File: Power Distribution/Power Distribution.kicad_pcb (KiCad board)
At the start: 4 copper layers, 60 x 82 mm, 81 parts, among them J1 Batt_Connector, J2 Motor Connector 1, J3 Motor Connector 2, J4 Motor Connector 3, J5 Motor Connector 3, U1 TPS552892RYQR, U2 TPS552892RYQR, U3 TPS552892RYQR, U4 TPS552892RYQR

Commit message: fixed via's
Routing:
- added copper zone on F.Cu, net Net-(U1-EXTVCC)
- added copper zone on F.Cu, net Net-(U3-EXTVCC)
- added copper zone on F.Cu, net Net-(U4-EXTVCC)

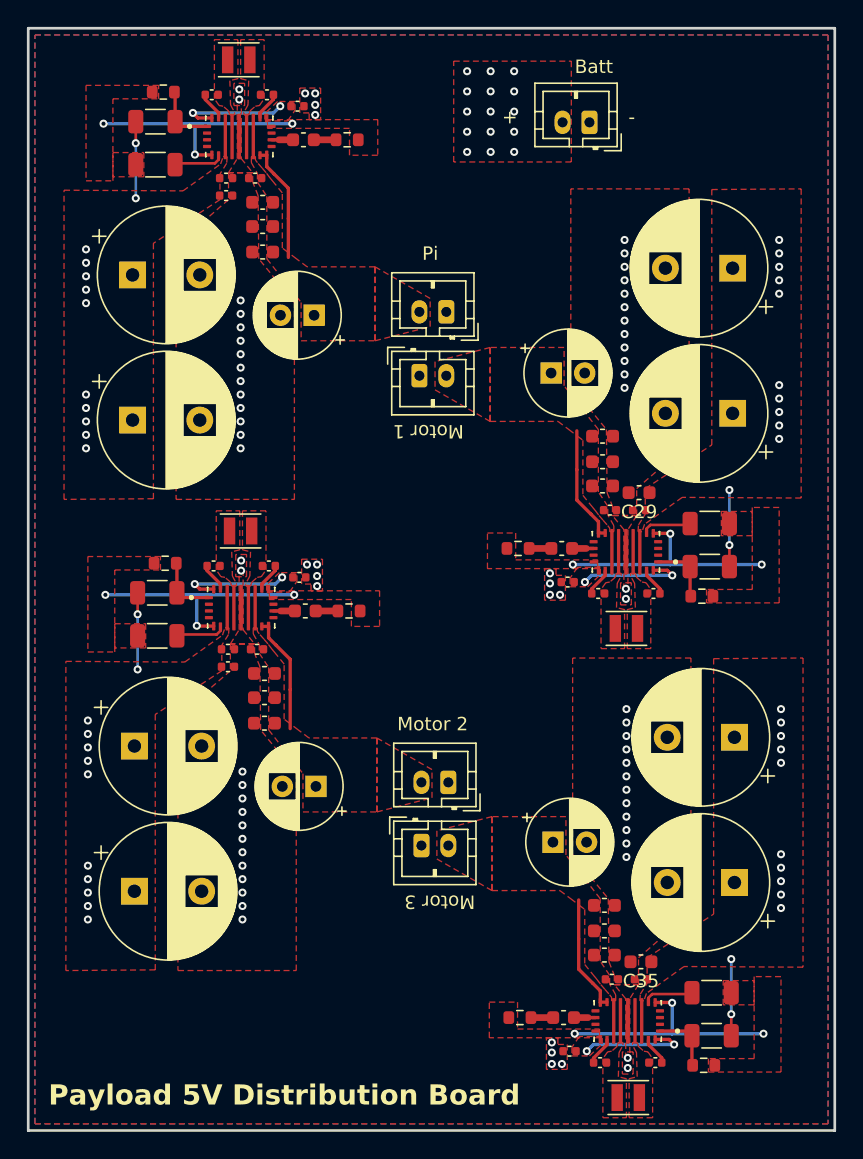
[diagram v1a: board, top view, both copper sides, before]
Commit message: added fabs and fixed i2c loop
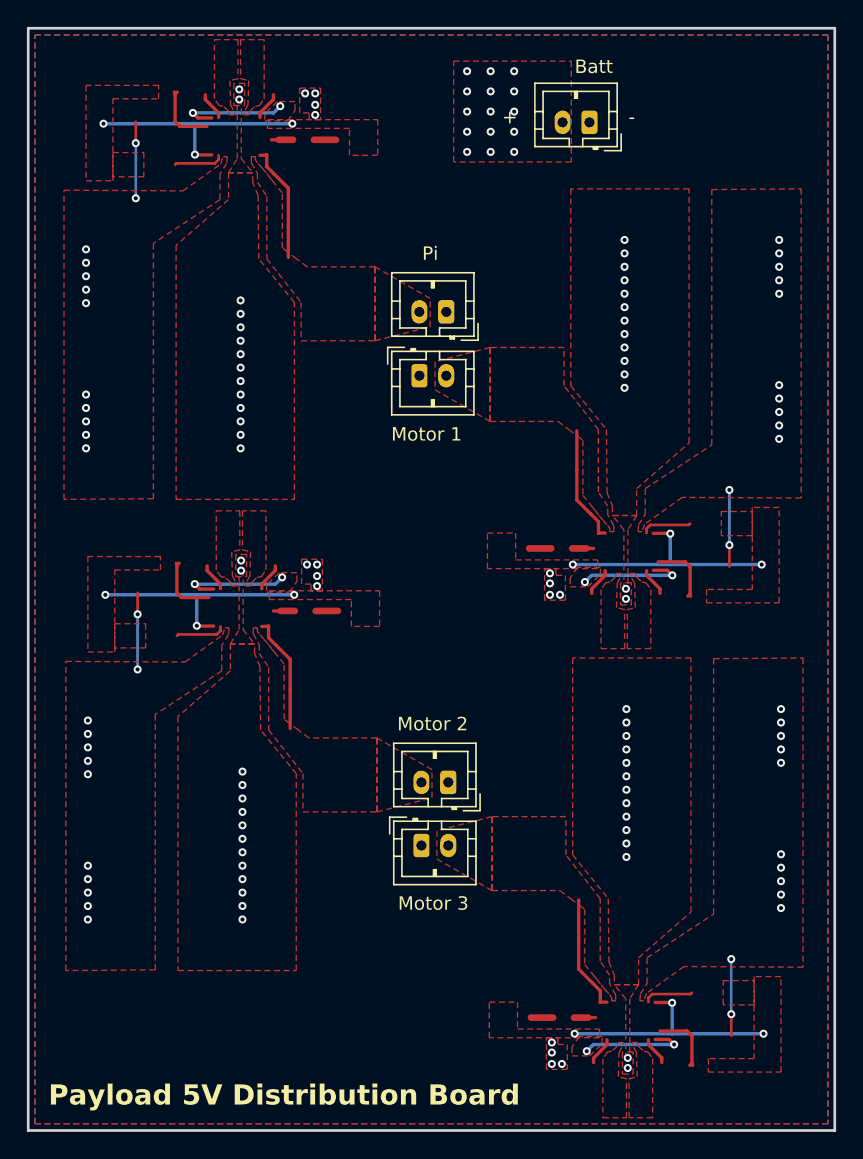
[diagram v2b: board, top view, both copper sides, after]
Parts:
- removed C1, C2, C27, C28, C3, C33, C34, C4: 100nF, Capacitor_SMD:C_0402_1005Metric
- removed C10, C11, C12, C31, C32, C37, C38, C9: 82µF, Capacitor_THT:CP_Radial_D10.0mm_P5.00mm
- removed C13, C18, C30, C36, C39, C45, C6, C8: 1µF, Capacitor_SMD:C_0402_1005Metric
- removed C14, C15, C16, C19, C20, C21, C40, C41, C42, C46, C47, C48: 22µF, Capacitor_SMD:C_0603_1608Metric
- removed C17, C22, C43, C49: 270µF, Capacitor_THT:CP_Radial_D6.3mm_P2.50mm
- removed C23, C24, C44, C50: 56nF, Capacitor_SMD:C_0603_1608Metric
- removed C25, C26, C51, C52: 4.7µF, Capacitor_SMD:C_0402_1005Metric
- removed C29, C35: 10µF, Capacitor_SMD:C_0603_1608Metric
- removed C5, C7: 10µF, Capacitor_SMD:C_0402_1005Metric
- removed L1, L2, L3, L4: 4.7µH, Inductor_SMD:L_Changjiang_FNR252010S
- removed R1, R10, R2, R9: 221k, Resistor_SMD:R_1206_3216Metric
- removed R11, R12, R3, R4: 100k, Resistor_SMD:R_0603_1608Metric
- removed R13, R15, R5, R7: 48.7k, Resistor_SMD:R_1206_3216Metric
- removed R14, R16, R6, R8: 301, Resistor_SMD:R_0603_1608Metric
- removed U1, U2, U3, U4: TPS552892RYQR, Package_TO_SOT_SMD:CONV_TPS552892RYQR
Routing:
- net (no net): track 0.00 -> 97.7 mm, vias 0 -> 8
- net Net-(U4-EXTVCC): track 8.27 -> 0.00 mm, vias 2 -> 0
- net Net-(U3-EXTVCC): track 8.27 -> 0.00 mm, vias 2 -> 0
- net Net-(U2-EXTVCC): track 8.27 -> 0.00 mm, vias 2 -> 0
- net Net-(U1-EXTVCC): track 8.27 -> 0.00 mm, vias 2 -> 0
- net Net-(U2-EN/UVLO): track 4.97 -> 0.00 mm
- net Net-(U4-EN/UVLO): track 4.97 -> 0.00 mm
- net Net-(U1-EN/UVLO): track 4.97 -> 0.00 mm
- net Net-(U3-EN/UVLO): track 4.97 -> 0.00 mm
- net Net-(U3-FSW): track 3.72 -> 0.00 mm
- net Net-(U1-FSW): track 3.72 -> 0.00 mm
- net Net-(U4-FSW): track 3.72 -> 0.00 mm
- net Net-(U2-FSW): track 3.72 -> 0.00 mm
- net Net-(U3-BOOT2): track 2.11 -> 0.00 mm
- net Net-(U2-BOOT2): track 2.11 -> 0.00 mm
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- added copper zone on F.Cu, net (none)
- removed copper zone on F.Cu, net Net-(U1-EXTVCC)
- removed copper zone on F.Cu, net Net-(U1-SW1)
- removed copper zone on F.Cu, net Net-(U1-SW2)
- removed copper zone on F.Cu, net Net-(U2-EXTVCC)
- removed copper zone on F.Cu, net Net-(U2-SW1)
- removed copper zone on F.Cu, net Net-(U2-SW2)
- removed copper zone on F.Cu, net Net-(U3-EXTVCC)
- removed copper zone on F.Cu, net Net-(U3-SW1)
- removed copper zone on F.Cu, net Net-(U3-SW2)
- removed copper zone on F.Cu, net Net-(U4-EXTVCC)
- removed copper zone on F.Cu, net Net-(U4-SW1)
- removed copper zone on F.Cu, net Net-(U4-SW2)
